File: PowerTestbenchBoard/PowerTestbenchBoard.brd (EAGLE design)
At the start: 160 x 100 mm, 2 parts, among them J8 182-037-213R531, J9 182-025-213R531

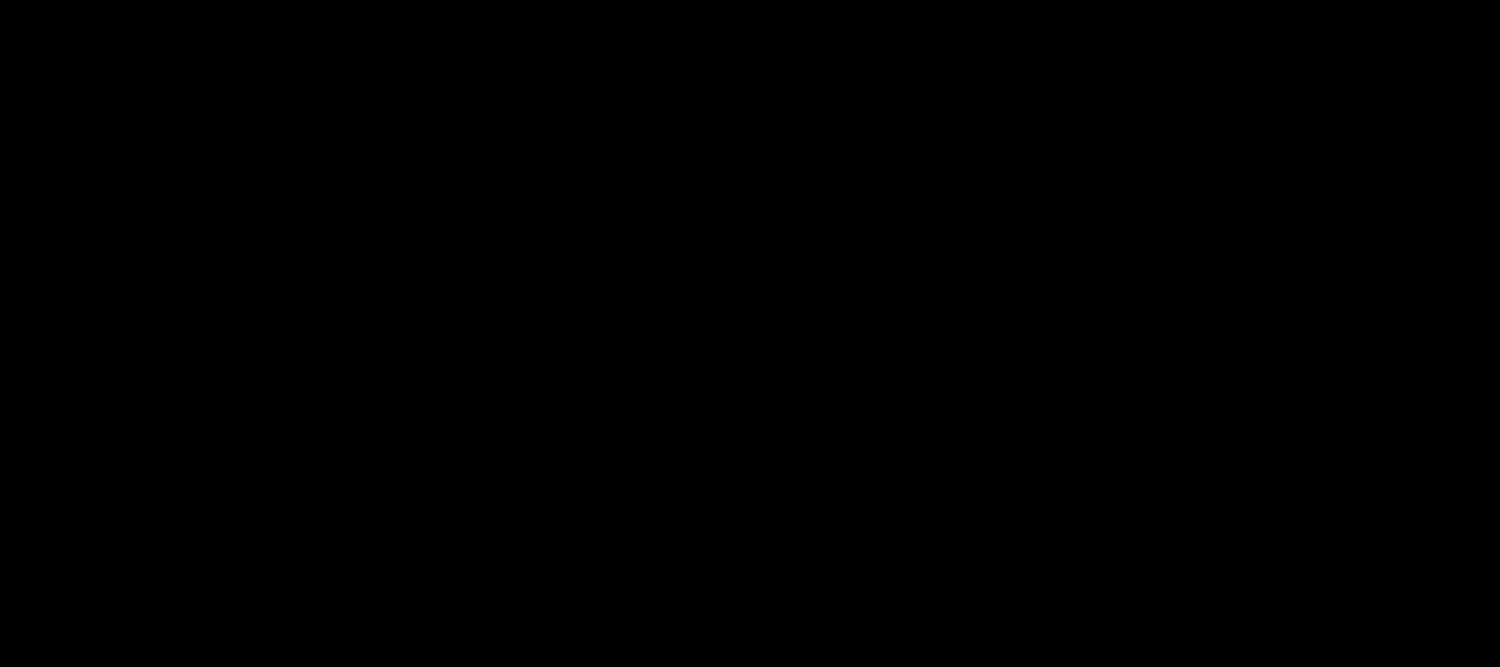
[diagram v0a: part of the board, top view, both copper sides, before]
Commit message: Started power test bench schem, mostly done
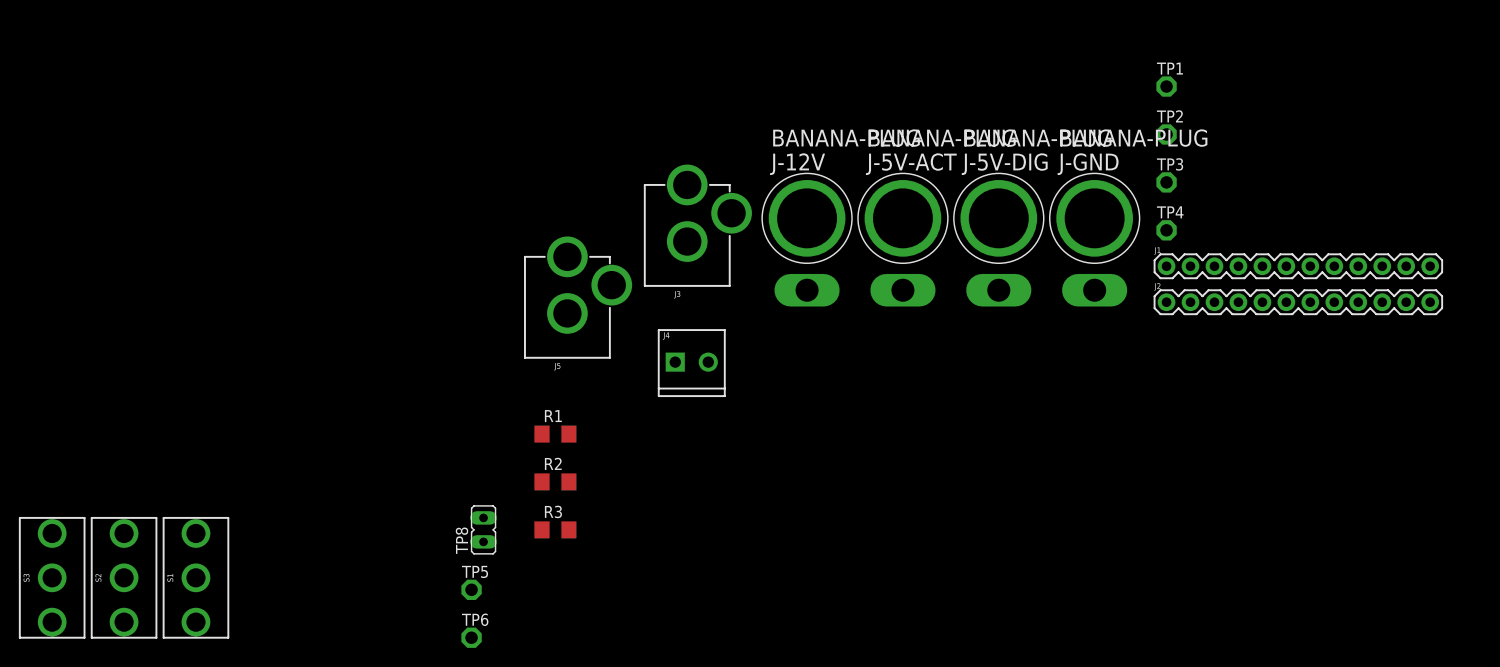
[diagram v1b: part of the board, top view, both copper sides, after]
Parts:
- added J-12V, J-5V-ACT, J-5V-DIG, J-GND: BANANA-PLUG, PowerManagementParts:BANANA-JACK
- added J1, J2: (no value), SparkFun-Connectors:1X12
- added J3, J5: POWER_JACK, SparkFun-Connectors:POWER_JACK_PTH
- added J4: (no value), SparkFun-Connectors:SCREWTERMINAL-3.5MM-2
- added R1, R2, R3: 0.1, rcl:R1206
- added S1, S2, S3: SPDT-SWITCH, PowerManagementParts:SWITCH_SPDT_PTH_11.6X4.0MM
- added TP1, TP2, TP3, TP4, TP5, TP6: TPPAD1-13, testpad:P1-13
- added TP8: (no value), jumper:JP1
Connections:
- removed net 12V-CAM: J8.25
- removed net 12V-STA: J8.14
- removed net 5V-ACT-CAM: J8.24
- removed net 5V-ACT-LASER: J8.3
- removed net 5V-ACT-MAG: J8.19
- removed net 5V-ACT-STA: J8.13
- removed net 5V-ACT-TX: J8.28
- removed net 5V-DIG-CAM: J8.23, J9.24
- removed net 5V-DIG-LASER: J8.2, J9.21
- removed net 5V-DIG-STA: J8.12, J9.22
- removed net CAM-USB-D+: J8.35, J9.18
- new net 12V: J2.1, J8.14, J8.25, R3.2, TP4.TP
- new net 12V-IN: J-12V.P$1, J-12V.P$2, J4.2, S3.2
- new net 5V-ACT: J2.2, J8.13, J8.19, J8.24, J8.28, J8.3, R2.2, TP3.TP
- new net 5V-ACT-IN: J-5V-ACT.P$1, J-5V-ACT.P$2, J3.PWR
- new net 5V-DIG: J2.3, J8.12, J8.18, J8.2, J8.23, J8.27, J9.21, J9.22, J9.24, R1.2, TP2.TP
- new net 5V-DIG-IN: J-5V-DIG.P$1, J-5V-DIG.P$2, J5.PWR, S1.2
- new net CAM-USB-D_N: J2.5
- new net CAM-USB-D_P: J2.6, J8.35, J9.18
- new net N$1: R1.1, S1.1
- new net N$2: R2.1, S2.1
- new net N$3: R3.1, S3.1
- net 5V-DIG-MAG: no longer J8.18
- net 5V-DIG-TX: no longer J8.27
- net ANT-MISO: now also J2.9
- net ANT-MOSI: now also J2.10
- net ANT-SCK: now also J2.8
- net ANT-SS: now also J2.7
- net BOOM-I2C-SCL: now also J2.11
- net BOOM-I2C-SDA: now also J2.12
- net GND: now also J-GND.P$1, J-GND.P$2, J2.4, J3.GND, J3.GNDBREAK, J4.1, J5.GND, J5.GNDBREAK, TP1.TP, TP5.TP, TP6.TP, TP8.1, TP8.2
- net LASER-I2C-SCL: now also J1.6
- net LASER-I2C-SDA: now also J1.7
- net LASER-UART-1: now also J1.12
- net LASER-UART-2: now also J1.11
- net LASER-UART-3: now also J1.10
- net LASER-UART-4: now also J1.9
- net LASER-UART-5: now also J1.8
- net MAGNET-I2C-SCL: now also J1.2
- net MAGNET-I2C-SDA: now also J1.3
- net STATIC-I2C-SCL: now also J1.4
- net STATIC-I2C-SDA: now also J1.5

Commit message: Board mostly routed. Added indicator LEDs and protection diodes
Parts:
- added D1, D4, D5: (no value), SparkFun-LED:LED_3MM-NS
- added D2, D3: 5.7V Zener, PowerManagementParts:SMB
- added H1, H2, H3, H4: MOUNT-HOLE3.3, holes:3,3
- added J6: (no value), SparkFun-Connectors:1X04
- added R4, R5: 330Ω, rcl:R0805
- added R6: 1.2kΩ, rcl:R0805
- added TP10, TP11, TP12, TP13, TP7, TP9: TPPAD1-13, testpad:P1-13
- J2: device SparkFun-Connectors:1X12 -> SparkFun-Connectors:1X02
- R1, R2, R3: value 0.1 -> 0.1Ω
- moved S3 248.9 mm to (25.4, 22.9), turned to 270 degrees
- moved S2 247.7 mm to (25.4, 35.6), turned to 270 degrees
- moved S1 247.4 mm to (25.4, 48.3), turned to 270 degrees
- moved J5 242.1 mm to (50.8, 80.0), turned to 180 degrees
- moved TP8 223.2 mm to (12.7, 71.1)
- moved R1 217.8 mm to (38.1, 48.3)
- moved J3 215.2 mm to (35.6, 80.0), turned to 180 degrees
- moved R2 214.5 mm to (38.7, 35.6)
- moved R3 210.8 mm to (38.7, 22.9)
- moved J4 203.9 mm to (22.9, 71.1), turned to 180 degrees
- moved TP4 197.4 mm to (77.5, 71.1), turned to 90 degrees
- moved TP6 193.3 mm to (12.7, 6.35)
- moved TP3 191.3 mm to (73.7, 71.1), turned to 90 degrees
- moved TP5 188.8 mm to (12.7, 1.91)
- moved J1 187.7 mm to (89.3, 27.2), turned to 90 degrees
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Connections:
- removed net 5V-DIG-MAG: J9.23
- removed net 5V-DIG-TX: J9.25
- removed net CAM-USB-D-: J8.36, J9.19
- new net N$4: D4.K, R4.2
- new net N$5: D5.K, R6.2
- new net N$6: D1.K, R5.2
- net 12V: now also D5.A, TP13.TP; no longer J2.1, TP4.TP
- net 12V-IN: now also TP4.TP
- net 5V-ACT: now also D2.C, D4.A, TP9.TP; no longer J2.2, TP3.TP
- net 5V-ACT-IN: now also S2.2, TP3.TP
- net 5V-DIG: now also D1.A, D3.C, J9.23, J9.25, TP11.TP; no longer J2.3, TP2.TP
- net 5V-DIG-IN: now also TP2.TP
- net ANT-MISO: now also J6.3; no longer J2.9
- net ANT-MOSI: now also J6.4; no longer J2.10
- net ANT-SCK: now also J6.2; no longer J2.8
- net ANT-SS: now also J6.1; no longer J2.7
- net BOOM-I2C-SCL: now also J2.1; no longer J2.11
- net BOOM-I2C-SDA: now also J2.2; no longer J2.12
- net CAM-USB-D_N: now also J8.36, J9.19; no longer J2.5
- net CAM-USB-D_P: no longer J2.6
- net GND: now also D2.A, D3.A, R4.1, R5.1, R6.1; no longer J2.4
- net N$1: now also TP10.TP
- net N$2: now also TP7.TP
- net N$3: now also TP12.TP
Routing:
- net 12V-IN: track 0.00 -> 141.2 mm
- net 5V-DIG: track 0.00 -> 108.4 mm
- net 5V-ACT-IN: track 0.00 -> 105.0 mm
- net MAGNET-I2C-SDA: track 0.00 -> 100.5 mm
- net LASER-UART-1: track 0.00 -> 95.5 mm, vias 0 -> 1
- net MAGNET-I2C-SCL: track 0.00 -> 94.4 mm
- net LASER-UART-2: track 0.00 -> 89.7 mm, vias 0 -> 1
- net 5V-ACT: track 0.00 -> 89.2 mm
- net LASER-UART-3: track 0.00 -> 85.1 mm, vias 0 -> 1
- net ANT-MOSI: track 0.00 -> 84.6 mm
- net LASER-UART-4: track 0.00 -> 80.5 mm, vias 0 -> 1
- net STATIC-I2C-SCL: track 0.00 -> 80.0 mm, vias 0 -> 1
- net ANT-MISO: track 0.00 -> 79.8 mm
- net STATIC-I2C-SDA: track 0.00 -> 79.6 mm, vias 0 -> 1
- net 5V-DIG-IN: track 0.00 -> 78.9 mm
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- added copper zone on layer 1, net 5V-DIG
- added copper zone on layer 16, net GND
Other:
- board size 160 x 100 mm -> 101.6 x 76.2 mm

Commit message: routed protection diodes
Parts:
- moved R5 112.4 mm to (42.5, 54.0), turned to 180 degrees
- moved R4 99.4 mm to (42.5, 41.3), turned to 180 degrees
- moved R6 96.0 mm to (41.9, 28.6), turned to 180 degrees
- moved D1 95.8 mm to (37.5, 54.0)
- moved D3 92.2 mm to (48.9, 45.7), turned to 270 degrees
- moved D4 88.4 mm to (37.5, 41.3)
- moved D5 82.5 mm to (37.5, 28.6)
- moved D2 75.7 mm to (48.9, 29.8), turned to 270 degrees
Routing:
- net 5V-ACT: track 89.2 -> 102.4 mm
- net 5V-DIG: track 108.4 -> 118.2 mm
- net GND: track 7.62 -> 17.0 mm, vias 0 -> 5
- net 12V: track 21.0 -> 29.0 mm
- net N$6: track 0.00 -> 2.86 mm
- net N$4: track 0.00 -> 2.86 mm
- net N$5: track 0.00 -> 2.23 mm

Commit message: Ready to manufacture
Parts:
- removed TP6: TPPAD1-13, testpad:P1-13
- moved D2 6.36 mm to (48.6, 36.2), turned to 90 degrees
- moved TP8 1.27 mm to (12.7, 72.4), turned to 90 degrees
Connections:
- net GND: now also J1.1; no longer TP6.TP
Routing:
- net LASER-UART-1: track 95.5 -> 94.4 mm
- net GND: track 17.0 -> 17.6 mm, vias 5 -> 4
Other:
- board text added: "12V"
- board text added: "5V-ACT"
- board text added: "5V-DIG"
- board text added: "ANT-MOSI ANT-MISO ANT-SCK ANT-SS"
- board text added: "Boom-SDA Boom-SCL"
- board text added: "GND"
- board text added: "Laser"
- board text added: "Magnet"
- board text added: "ON OFF"
- board text added: "Static"
- board text added: "UART1 UART2 UART3 UART4 UART5 SDA SCL SDA SCL SDA SCL GND"
